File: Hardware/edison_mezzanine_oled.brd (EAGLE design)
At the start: 30.5 x 44.5 mm, 26 parts, among them J1 EDISON_CONNECTOR_FULLMOUNTING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, J2 EDISON_CONNECTOR_FULLHEADER

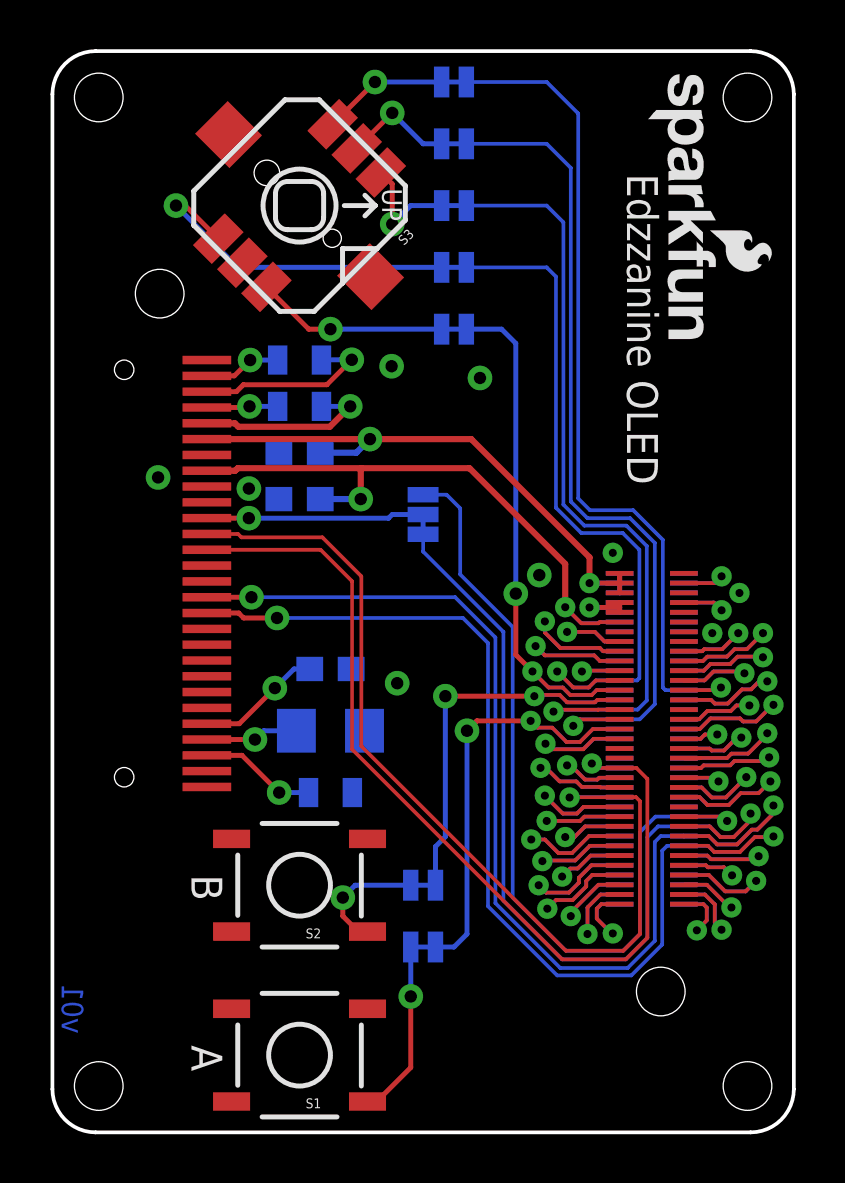
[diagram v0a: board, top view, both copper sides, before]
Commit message: Removing top-side mezzanine connector
Rerouting, increasing minimum trace width to 8mil, upping via drills to
20mil.
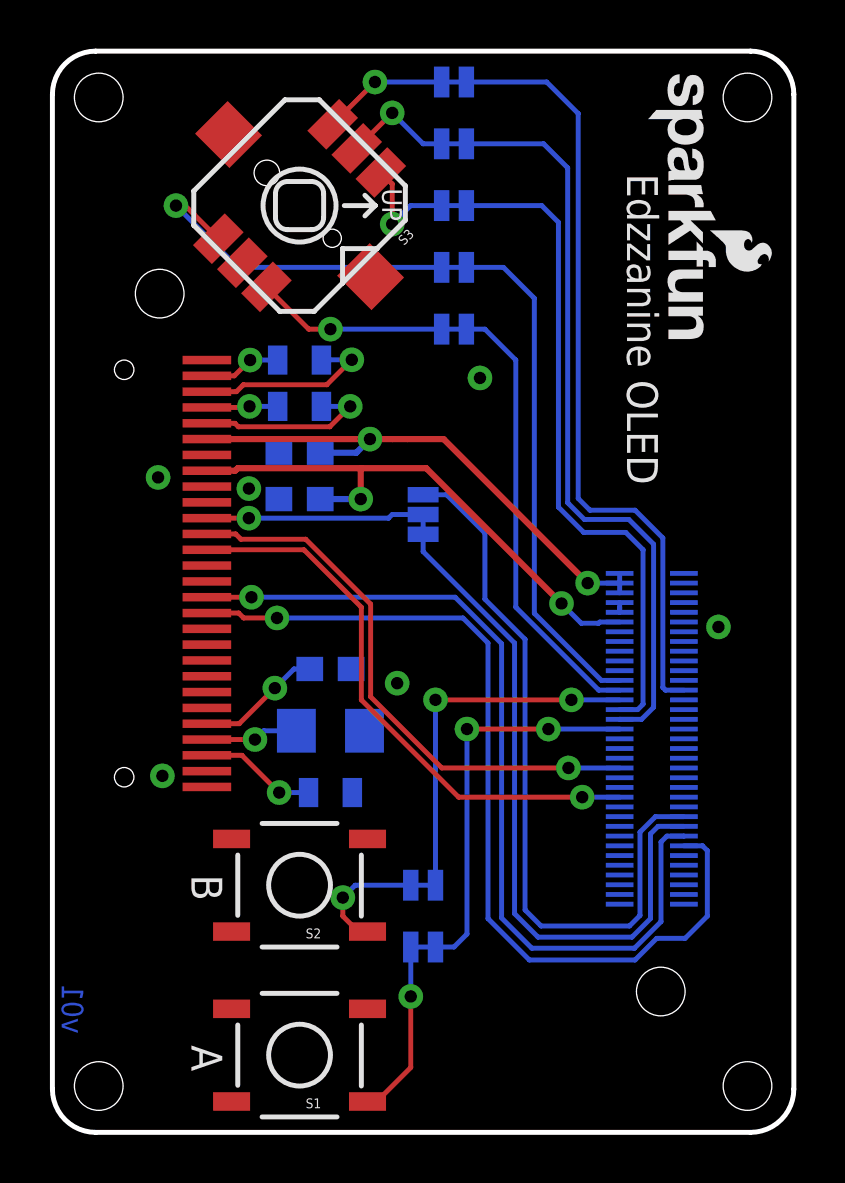
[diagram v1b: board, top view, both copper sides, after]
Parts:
- removed J2: EDISON_CONNECTOR_FULLHEADER, Edison:DF40C-70DP-0.4(51)
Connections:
- net 1.8V: no longer J2.12
- net 3.3V: no longer J2.10, J2.8
- net FAULT: no longer J2.19
- net FW_RCVR: no longer J2.69
- net GND: no longer J2.1, J2.11, J2.13, J2.15, J2.5, J2.9
- net GP109_SPI_2_CLK: no longer J2.55
- net GP110_SPI_2_FS0: no longer J2.53
- net GP111_SPI_2_FS1: no longer J2.51
- net GP114_SPI_2_RXD: no longer J2.59
- net GP115_SPI_2_TXD: no longer J2.57
- net GP128_UART_1_CTS: no longer J2.65
- net GP129_UART_1_RTS: no longer J2.63
- net GP12_PWM0: no longer J2.35
- net GP130_UART_1_RX: no longer J2.61
- net GP131_UART_1_TX: no longer J2.46
- net GP134_UART_2_RX: no longer J2.22
- net GP135_UART_2_TX: no longer J2.27
- net GP13_PWM1: no longer J2.33
- net GP14: now also OLED1.13; no longer J2.48, OLED1.12
- net GP15: now also OLED1.12; no longer J2.42, OLED1.13
- net GP165: no longer J2.25
- net GP182_PWM2: no longer J2.37
- net GP183_PWM3: no longer J2.39
- net GP19_I2C_1_SCL: no longer J2.41
- net GP20_I2C_1_SDA: no longer J2.43
- net GP27_I2C_6_SCL: no longer J2.45
- net GP28_I2C_6_SDA: no longer J2.47
- net GP40_I2S_2_CLK: no longer J2.52
- net GP41_I2S_2_FS: no longer J2.54
- net GP42_I2S_2_RXD: no longer J2.50
- net GP43_I2S_2_TXD: no longer J2.56
- net GP44: no longer J2.24
- net GP45: no longer J2.26
- net GP46: no longer J2.28
- net GP47: no longer J2.30
- net GP48: no longer J2.32
- net GP49: no longer J2.34
- net GP77_SD_0_CD#: no longer J2.60
- net GP78_SD_0_CLK: no longer J2.58
- net GP79_SD_0_CMD: no longer J2.62
- net GP80_SD_0_DAT0: no longer J2.66
- net GP81_SD_0_DAT1: no longer J2.70
- net GP82_SD_0_DAT2: no longer J2.64
- net GP83_SD_0_DAT3: no longer J2.68
- net GP84_SD_CLK_FB: no longer J2.44
- net MSIC_SLP_CLK: no longer J2.7
- net OSC_CLK_OUT: no longer J2.67
- net PSW: no longer J2.21
- net PWRBTN#: no longer J2.17
- net RCVR_MODE: no longer J2.31
- net RESET_OUT#: no longer J2.36
- net USB_DN: no longer J2.18
- net USB_DP: no longer J2.16
- net USB_ID: no longer J2.3
- net USB_VBUS: no longer J2.20
- net VSYS: no longer J2.2, J2.4, J2.6
- net V_BAT_BKUP: no longer J2.23
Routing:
- net GP15: track 39.8 -> 23.2 mm
- net GP14: track 39.8 -> 23.4 mm
- net GP109_SPI_2_CLK: track 46.3 -> 36.0 mm, vias 2 -> 1
- net GP44: track 29.5 -> 20.9 mm, vias 1 -> 0
- net GP13_PWM1: track 8.40 -> 0.00 mm, vias 1 -> 0
- net GP43_I2S_2_TXD: track 8.31 -> 0.00 mm, vias 1 -> 0
- net GP28_I2C_6_SDA: track 8.17 -> 0.00 mm, vias 1 -> 0
- net GP79_SD_0_CMD: track 8.08 -> 0.00 mm, vias 1 -> 0
- net GP110_SPI_2_FS0: track 36.5 -> 28.4 mm, vias 1 -> 0
- net GP183_PWM3: track 7.77 -> 0.00 mm, vias 1 -> 0
- net GP135_UART_2_TX: track 7.74 -> 0.00 mm, vias 1 -> 0
- net USB_DN: track 7.70 -> 0.00 mm, vias 1 -> 0
- net FAULT: track 7.45 -> 0.00 mm, vias 1 -> 0
- net USB_VBUS: track 7.42 -> 0.00 mm, vias 1 -> 0
- net GP19_I2C_1_SCL: track 7.37 -> 0.00 mm, vias 1 -> 0
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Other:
- board text removed: "Connectors Go Here"
- board text removed: "LED's and selector switches go here"
- board text removed: "Max Board Length"
- board text removed: "Nothing goes here... I mean it."

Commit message: Moving OLED passives to top side
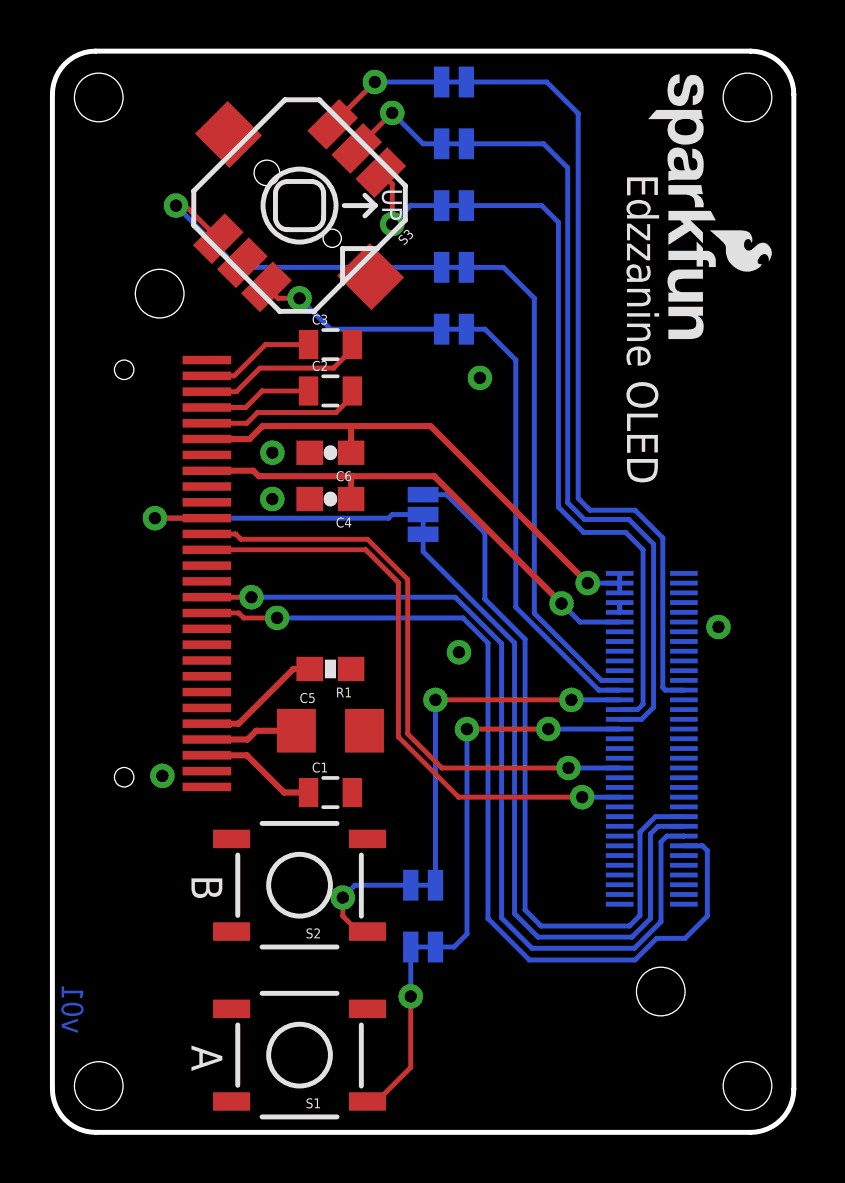
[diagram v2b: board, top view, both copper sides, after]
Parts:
- moved C2 1.42 mm to (11.4, 30.5), flipped to the top, turned to 0 degrees
- moved C3 1.42 mm to (11.4, 32.4), flipped to the top, turned to 0 degrees
- moved C4 1.27 mm to (11.4, 26.0), flipped to the top, turned to 180 degrees
- moved C6 1.27 mm to (11.4, 27.9), flipped to the top, turned to 180 degrees
- flipped C1 to the top, turned to 0 degrees
- flipped C5 to the top, turned to 0 degrees
- flipped R1 to the top, turned to 180 degrees
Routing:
- net OLED_!CS!: track 8.95 -> 13.2 mm
- net 1.8V: track 22.6 -> 20.5 mm, vias 2 -> 1
- net C1P: track 2.93 -> 4.46 mm, vias 1 -> 0
- net C2P: track 3.18 -> 4.71 mm, vias 1 -> 0
- net GP15: track 23.2 -> 24.7 mm
- net GP14: track 23.4 -> 24.9 mm
- net C2N: track 7.78 -> 6.89 mm, vias 1 -> 0
- net C1N: track 7.48 -> 6.66 mm, vias 1 -> 0
- net VSYS: track 22.5 -> 21.8 mm, vias 2 -> 1
- net IREF: vias 1 -> 0
- net VCOMH: vias 1 -> 0
- net VCC: vias 1 -> 0

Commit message: Moving screen closer towards middle of board
- Updating Edison package
- Moving Joystick and buttons towards middle of board.
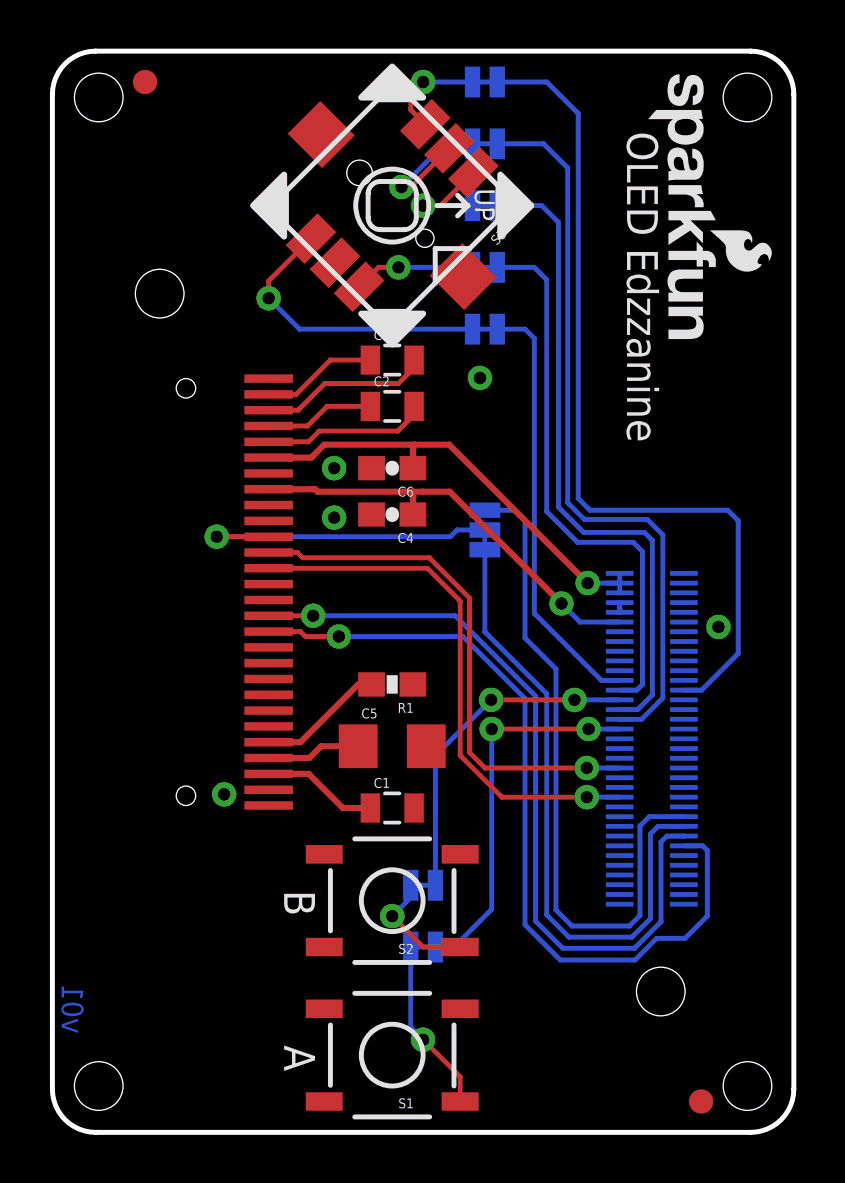
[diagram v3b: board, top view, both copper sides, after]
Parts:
- added FID1, FID2: FIDUCIAL1X2, SparkFun-Aesthetics:FIDUCIAL-1X2
- moved S2 3.86 mm to (14.0, 9.53)
- moved S1 3.81 mm to (14.0, 3.17)
- moved S3 3.81 mm to (14.0, 38.1)
- moved SJ4 2.84 mm to (17.8, 33.0)
- moved SJ6 2.84 mm to (17.8, 35.6)
- moved OLED1 2.65 mm to (8.89, 31.0)
- moved C1 2.62 mm to (14.0, 13.3)
- moved C2 2.62 mm to (14.0, 29.8)
- moved C4 2.62 mm to (14.0, 25.4)
- moved C5 2.62 mm to (14.0, 15.9)
- moved C6 2.62 mm to (14.0, 27.3)
- moved R1 2.62 mm to (14.0, 18.4)
- moved C3 2.62 mm to (14.0, 31.8)
- moved SJ2 2.62 mm to (17.8, 24.8)
- moved SJ3 1.27 mm to (17.8, 38.1)
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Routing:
- net GP45: track 18.4 -> 22.9 mm
- net GP115_SPI_2_TXD: track 37.6 -> 33.6 mm
- net GP109_SPI_2_CLK: track 36.0 -> 32.0 mm
- net GP44: track 20.9 -> 17.6 mm
- net VSYS: track 21.8 -> 18.8 mm
- net JOY_R: track 7.92 -> 4.99 mm
- net 1.8V: track 20.5 -> 17.6 mm
- net GP15: track 24.7 -> 21.8 mm
- net GP14: track 24.9 -> 22.0 mm
- net GP165: track 32.2 -> 35.0 mm
- net GP110_SPI_2_FS0: track 28.4 -> 26.0 mm
- net JOY_D: track 14.3 -> 12.1 mm
- net GP111_SPI_2_FS1: track 30.0 -> 27.9 mm
- net JOY_C: track 4.62 -> 6.29 mm
- net GP46: track 15.2 -> 13.9 mm
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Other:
- board text added: "OLED Edzzanine"
- board text removed: "Edzzanine OLED"

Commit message: adding fiducials to bottom side
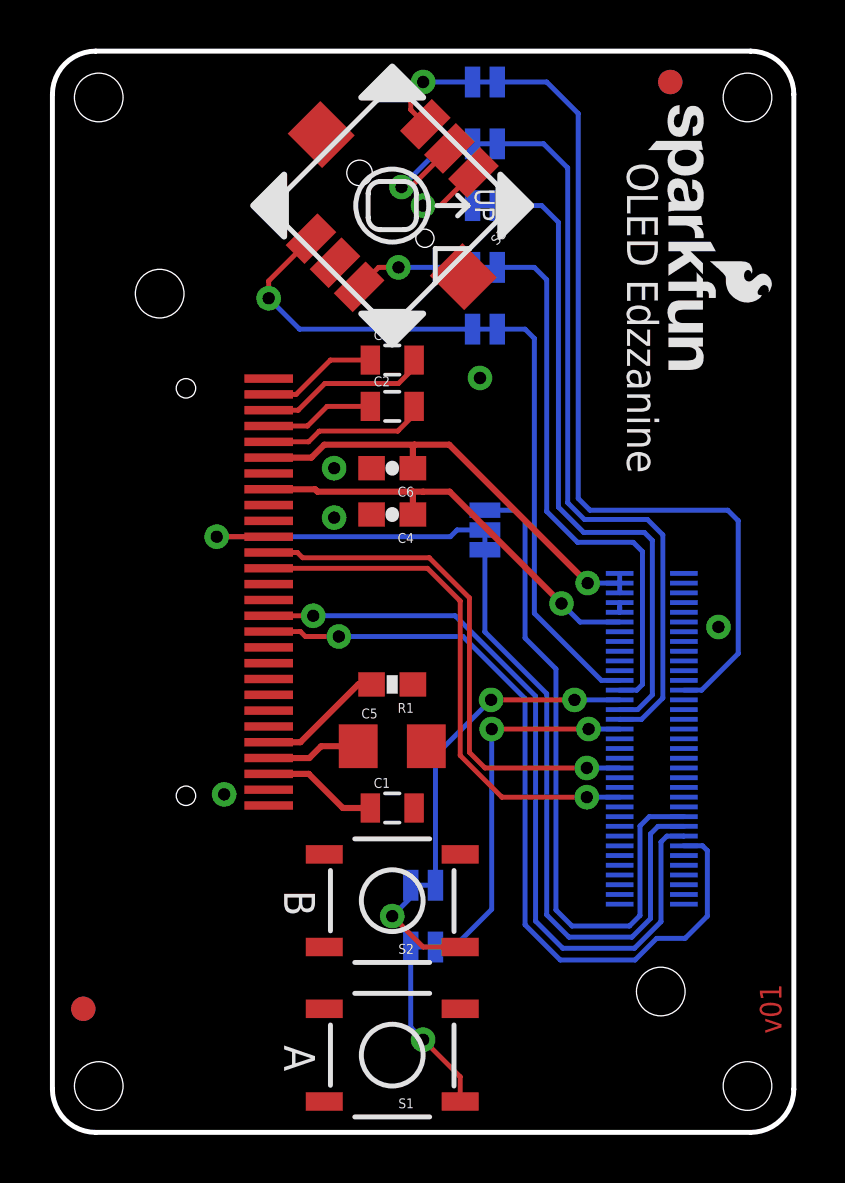
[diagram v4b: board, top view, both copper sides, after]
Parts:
- added FID3, FID4: FIDUCIAL1X2, SparkFun-Aesthetics:FIDUCIAL-1X2
- moved FID2 25.7 mm to (1.27, 5.08)
- moved FID1 21.6 mm to (25.4, 43.2), flipped to the bottom
- moved LOGO1 1.27 mm to (24.4, 42.7)
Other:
- board text removed: "Casey Kuhns"
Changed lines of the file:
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@@
 <wire x1="28.702" y1="0" x2="1.778" y2="0" width="0.2032" layer="20"/>
 <wire x1="0" y1="1.778" x2="0" y2="42.672" width="0.2032" layer="20"/>
-<text x="27.94" y="-13.97" size="1.6764" layer="51" ratio="15">Casey Kuhns</text>
 <hole x="28.575" y="1.905" drill="2"/>
 <hole x="1.905" y="1.905" drill="2"/>
@@
 <text x="10.795" y="3.048" size="1.27" layer="21" font="vector" ratio="15" rot="SR270" align="top-center">A</text>
 <text x="10.795" y="9.4234" size="1.27" layer="21" font="vector" ratio="15" rot="SR270" align="top-center">B</text>
-<text x="24.892" y="41.148" size="1.27" layer="21" font="vector" ratio="15" rot="SR270" align="top-left">OLED Edzzanine</text>
+<text x="24.892" y="39.878" size="1.27" layer="21" font="vector" ratio="15" rot="SR270" align="top-left">OLED Edzzanine</text>
 <text x="16.51" y="43.18" size="0.889" layer="22" font="vector" ratio="15" rot="MR180" align="center-right">L</text>
 <text x="16.51" y="40.64" size="0.889" layer="22" font="vector" ratio="15" rot="MR180" align="center-right">C</text>
@@
 <text x="18.8976" y="33.02" size="0.889" layer="22" font="vector" ratio="15" rot="MR0" align="center-right">44</text>
 <text x="18.8976" y="35.56" size="0.889" layer="22" font="vector" ratio="15" rot="MR0" align="center-right">45</text>
-<text x="1.27" y="5.08" size="0.889" layer="16" font="vector" ratio="15" rot="MR90" align="top-center">v01</text>
+<text x="29.972" y="5.08" size="0.889" layer="1" font="vector" ratio="15" rot="R270" align="top-center">v01</text>
 <text x="13.97" y="7.62" size="0.889" layer="22" font="vector" ratio="15" rot="MR180" align="center-right">A</text>
 <text x="13.97" y="10.16" size="0.889" layer="22" font="vector" ratio="15" rot="MR180" align="center-right">B</text>
 <text x="16.3576" y="10.16" size="0.889" layer="22" font="vector" ratio="15" rot="MR0" align="center-right">46</text>
 <text x="16.3576" y="7.62" size="0.889" layer="22" font="vector" ratio="15" rot="MR0" align="center-right">49</text>
-<text x="27.94" y="-16.51" size="1.6764" layer="51" ratio="15">Jim Lindblom</text>
+<text x="27.94" y="-13.97" size="1.6764" layer="51" ratio="15">Jim Lindblom</text>
 <polygon width="0.254" layer="21" spacing="0.6096">
 <vertex x="18.415" y="36.83"/>
@@
 <element name="SJ7" library="SparkFun-Passives" package="PAD-JUMPER-2-NC_BY_TRACE_YES_SILK" value="" x="17.78" y="40.64" rot="MR180"/>
 <element name="SJ8" library="SparkFun-Passives" package="PAD-JUMPER-2-NC_BY_TRACE_YES_SILK" value="" x="15.24" y="7.62" rot="MR180"/>
-<element name="LOGO1" library="SparkFun-Aesthetics" package="SFE_LOGO_NAME_FLAME_.1" value="SFE_LOGO_NAME_FLAME.1_INCH" x="24.384" y="43.942" rot="R270"/>
-<element name="FID1" library="SparkFun-Aesthetics" package="FIDUCIAL-1X2" value="FIDUCIAL1X2" x="3.81" y="43.18"/>
-<element name="FID2" library="SparkFun-Aesthetics" package="FIDUCIAL-1X2" value="FIDUCIAL1X2" x="26.67" y="1.27"/>
+<element name="LOGO1" library="SparkFun-Aesthetics" package="SFE_LOGO_NAME_FLAME_.1" value="SFE_LOGO_NAME_FLAME.1_INCH" x="24.384" y="42.672" rot="R270"/>
+<element name="FID1" library="SparkFun-Aesthetics" package="FIDUCIAL-1X2" value="FIDUCIAL1X2" x="25.4" y="43.18" rot="MR0"/>
+<element name="FID2" library="SparkFun-Aesthetics" package="FIDUCIAL-1X2" value="FIDUCIAL1X2" x="1.27" y="5.08"/>
+<element name="FID3" library="SparkFun-Aesthetics" package="FIDUCIAL-1X2" value="FIDUCIAL1X2" x="1.27" y="5.08" rot="MR0"/>
+<element name="FID4" library="SparkFun-Aesthetics" package="FIDUCIAL-1X2" value="FIDUCIAL1X2" x="25.4" y="43.18"/>
 </elements>
 <signals>
